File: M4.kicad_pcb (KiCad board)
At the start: 2 copper layers, 57.2 x 105 mm, 181 parts, among them J1 PJ-301B, J10 PJ-301B, J11 PJ-301B, J12 PJ-301B, J13 PJ-301B, J2 PJ-301B, J3 PJ-301B, J4 PJ-301B, J5 PJ-301B, J6 PJ-301B, J7 PJ-301B, J8 PJ-301B, J9 PJ-301B, P1 CONN_01X01, P2 CONN_01X01, P3 CONN_01X01, P4 CONN_01X01, P5 CONN_01X06, P6 CONN_02X05, P7 CONN_01X01, SW1 B3F-1050, SW2 B3F-1050, SW3 B3F-1050, SW4 B3F-1050, SW5 B3F-1050, SW6 B3F-1050, SW7 B3F-1050, U1 LM1117, U10 STM32F410RBTx, U2 MCP1703, U3 MAX5134, U4 74ACT541, U5 OPA4171, U6 OPA171, U7 OPA171, U8 CD4051, U9 OPA4171, X1 MIDI IN, Y1 8MHz

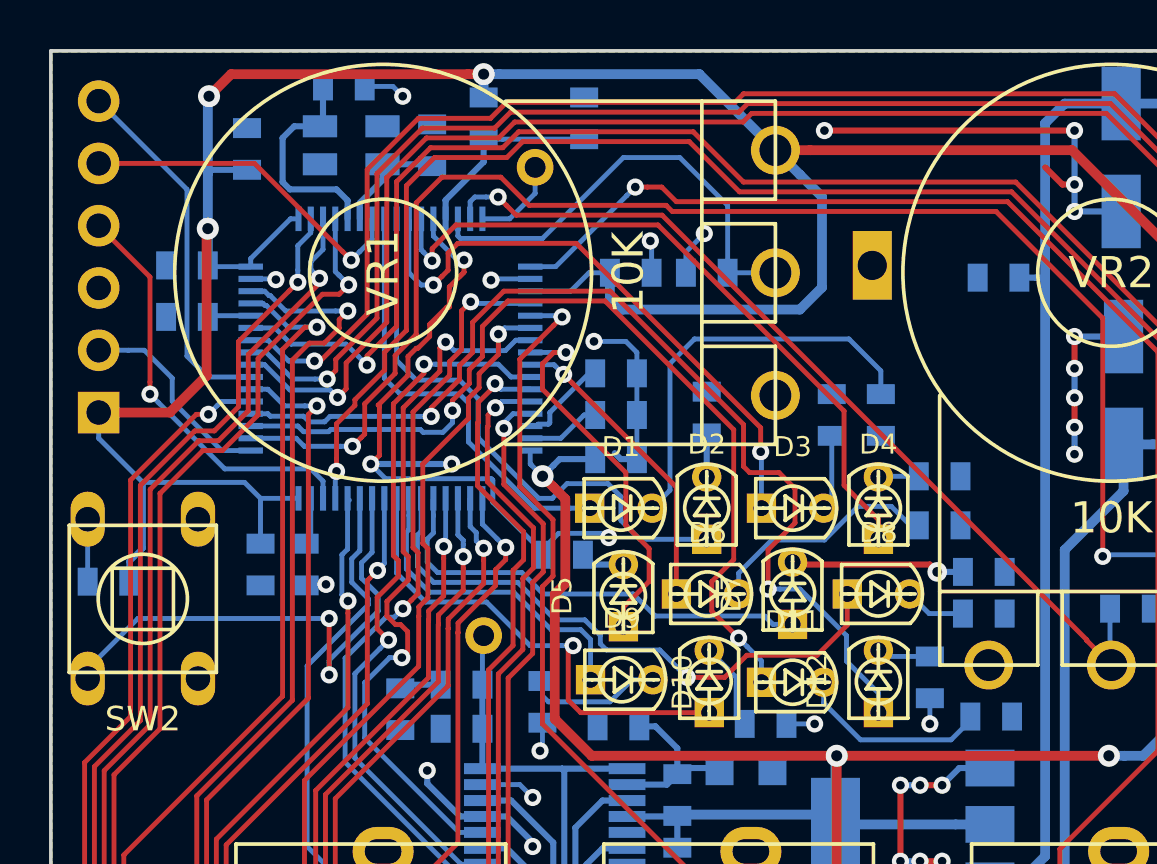
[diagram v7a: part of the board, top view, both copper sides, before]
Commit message: changed LED models to TLUGX240
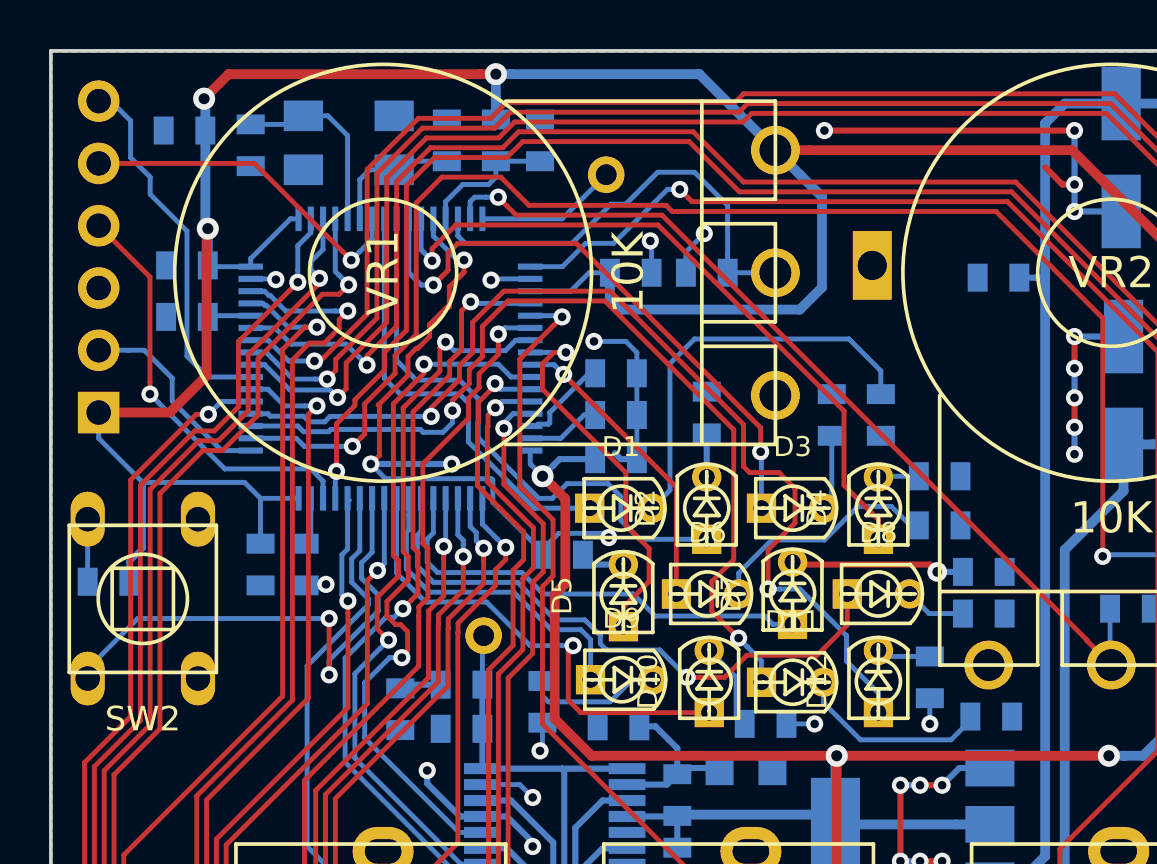
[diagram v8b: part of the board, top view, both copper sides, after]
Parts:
- Y1: value 8MHz -> 4-SMD-XTAL; footprint synth:403-XTAL-4-SMD -> MyModules:4-SMD-3.2X5.0MM_XTAL
- moved C14 4.49 mm to (114.9, 42.1), turned to 90 degrees
- moved P7 2.92 mm to (129.4, 43.3)
- moved C16 2.66 mm to (112.2, 41.5), turned to 180 degrees
- moved C32 2.01 mm to (126.7, 41.9)
- moved L2 1.03 mm to (124.9, 41.9)
- moved C15 0.63 mm to (122.9, 41.9)
- moved Y1 0.14 mm to (118.9, 42.0)
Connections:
- Y1 pad 2: Net-(C15-Pad2) -> (no net)
- Y1 pad 3: (no net) -> Net-(C15-Pad2)
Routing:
- net Net-(C32-Pad1): track 7.99 -> 5.61 mm
- net /PA2: track 3.64 -> 5.80 mm
- net GND: track 104.9 -> 103.2 mm, vias 42 -> 41
- net Net-(C14-Pad2): track 8.91 -> 7.83 mm
- net Net-(C15-Pad2): track 4.66 -> 5.46 mm
- net +3V3: track 346.8 -> 346.2 mm
